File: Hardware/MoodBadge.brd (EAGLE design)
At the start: 112.2 x 114.3 mm, 80 parts, among them IC1 PCF8574T, U2 ATMEGA328P_TQFP, Y1 Crystal-CA-310

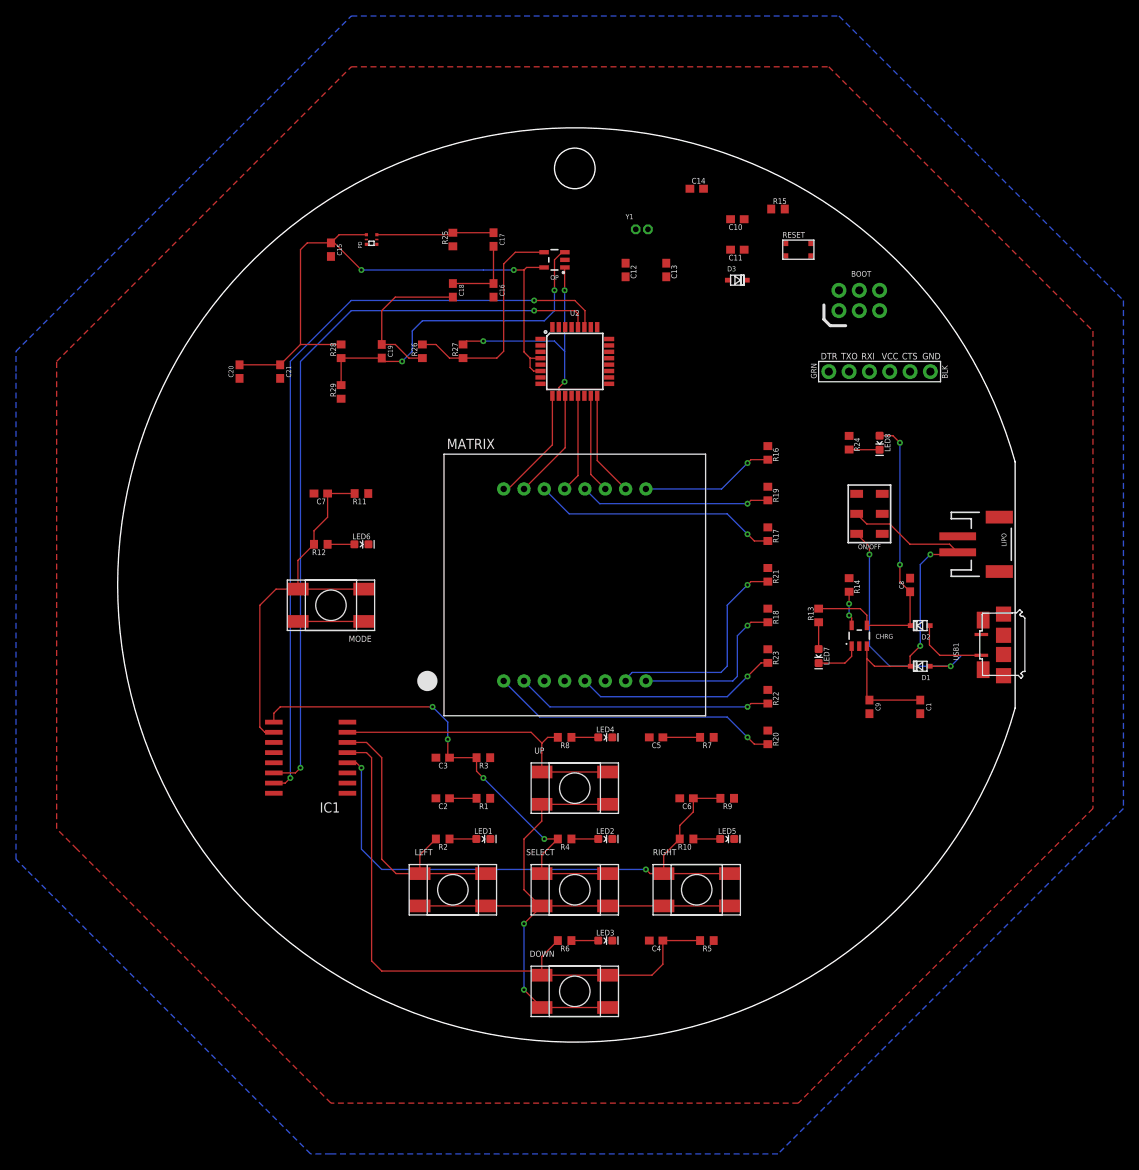
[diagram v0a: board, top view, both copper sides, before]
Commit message: Finished creating traces and filled copper pour
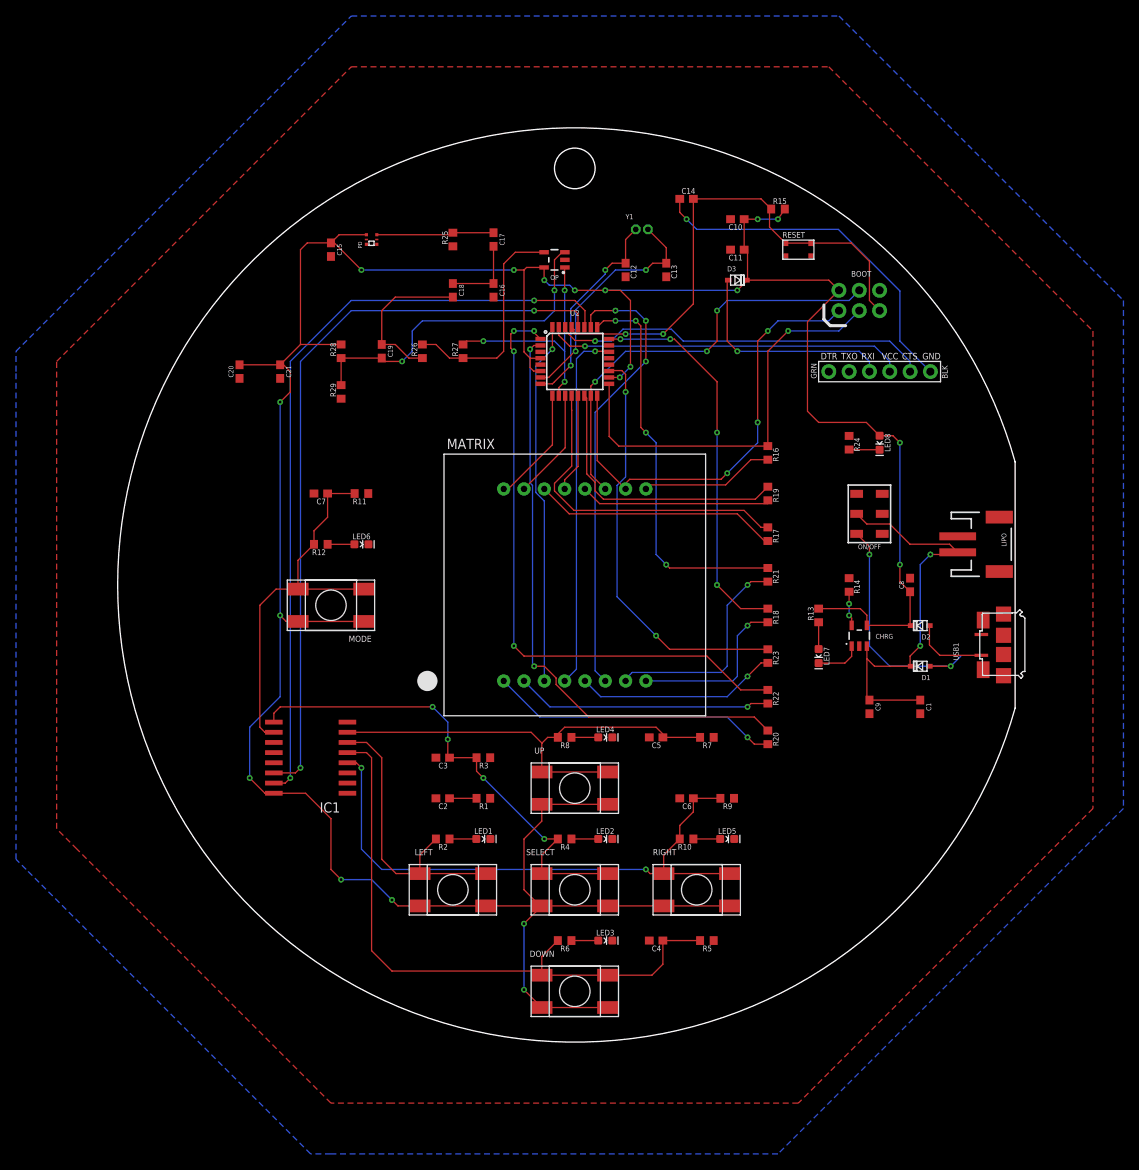
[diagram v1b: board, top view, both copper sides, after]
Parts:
- moved C14 1.80 mm to (14.0, 48.3)
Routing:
- net VCC: track 210.6 -> 395.3 mm, vias 6 -> 19
- net LD2: track 0.00 -> 77.6 mm, vias 0 -> 4
- net LD1: track 0.00 -> 74.3 mm, vias 0 -> 2
- net RESET: track 0.00 -> 64.2 mm, vias 0 -> 2
- net LD6: track 0.00 -> 57.3 mm, vias 0 -> 3
- net LD9: track 0.00 -> 52.3 mm, vias 0 -> 1
- net LD5: track 0.00 -> 52.1 mm, vias 0 -> 2
- net LD7: track 0.00 -> 50.1 mm, vias 0 -> 4
- net LD8: track 0.00 -> 48.7 mm, vias 0 -> 4
- net RXD: track 0.00 -> 47.8 mm, vias 0 -> 1
- net LD3: track 0.00 -> 45.5 mm, vias 0 -> 1
- net LD4: track 0.00 -> 45.4 mm, vias 0 -> 1
- net TXD: track 0.00 -> 45.0 mm, vias 0 -> 1
- net DTR: track 0.00 -> 44.9 mm, vias 0 -> 1
- net LD10: track 13.1 -> 56.9 mm, vias 0 -> 3
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
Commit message: Adjusted trace width and ran DRC
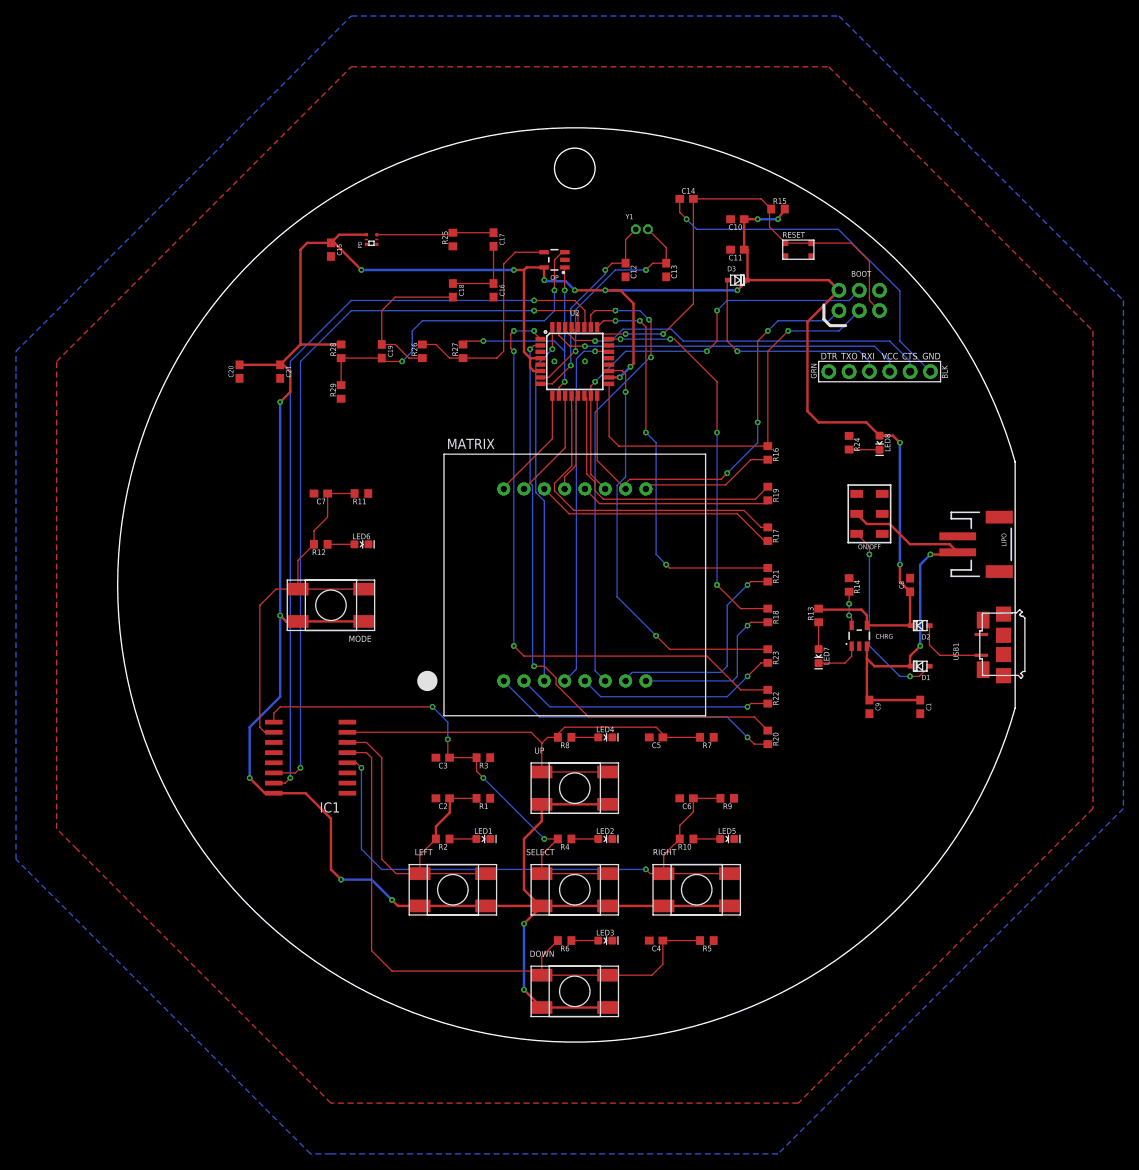
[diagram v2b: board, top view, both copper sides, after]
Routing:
- net N$2: track 30.3 -> 24.3 mm
- net LEFT: track 40.1 -> 45.9 mm
- net LD6: track 57.3 -> 58.2 mm

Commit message: Fixed labeling error for FTDI pins
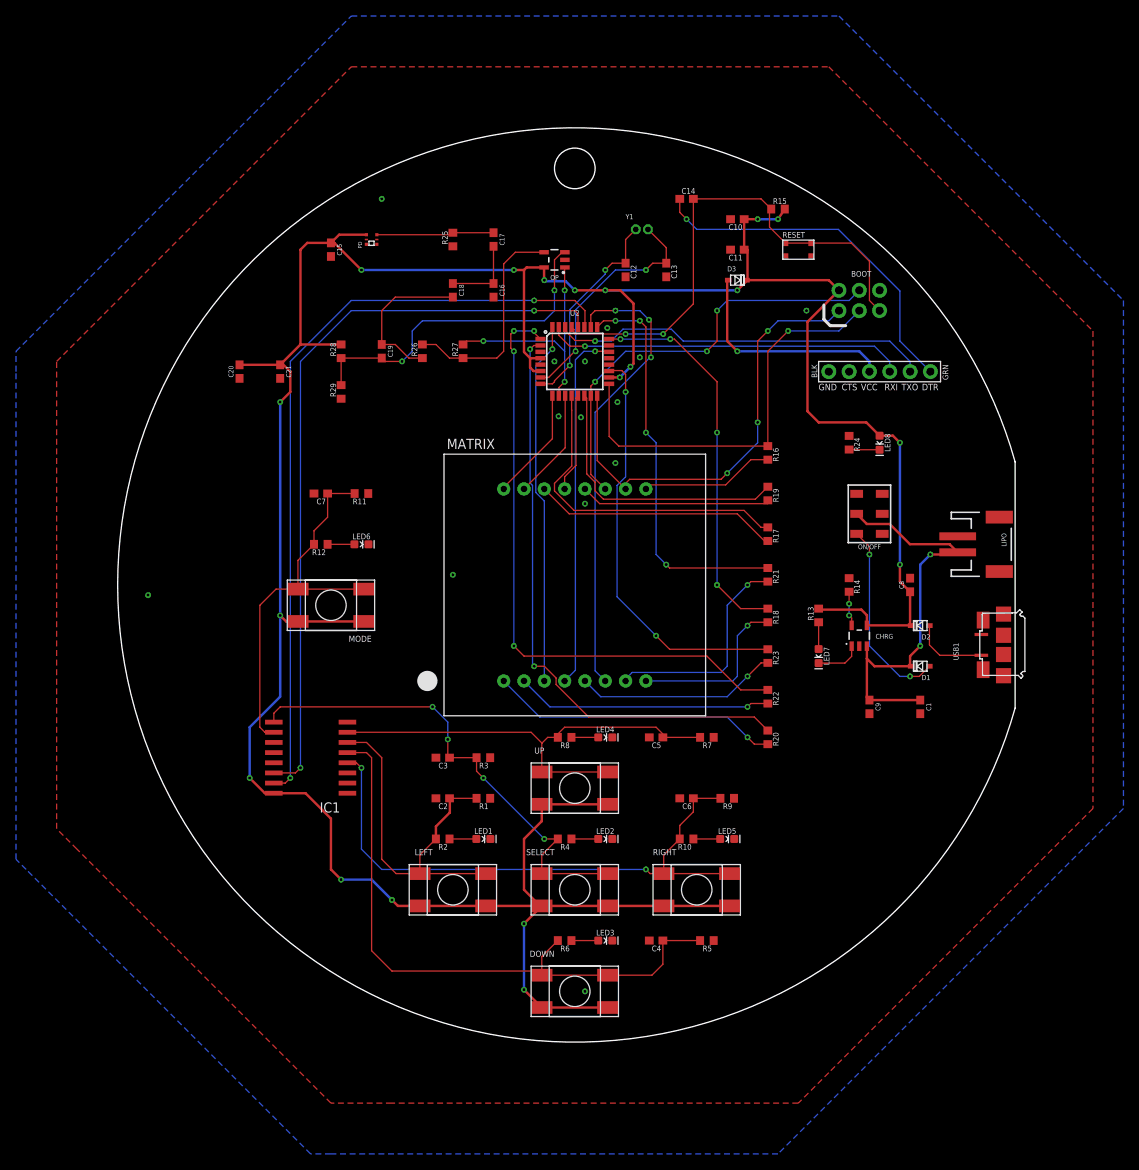
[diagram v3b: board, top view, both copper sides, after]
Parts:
- turned FTDI2 to 180 degrees
- renumbered FTDI1 to FTDI2
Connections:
- net DTR: now also FTDI2.DTR; no longer FTDI2.GND
- net GND: now also FTDI2.CTS, FTDI2.GND; no longer FTDI2.DTR, FTDI2.TXO
- net N$12: now also FTDI2.VCC; no longer FTDI2.RXI
- net RXD: now also FTDI2.TXO; no longer FTDI2.CTS
- net TXD: now also FTDI2.RXI; no longer FTDI2.VCC
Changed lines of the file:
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@@
 <attribute name="VALUE" x="19.05" y="36.435" size="0.635" layer="27"/>
 </element>
-<element name="FTDI1" library="LinnesLab-Connectors" package="FTDI_DEVICE" value="FTDI_DEVICE" x="38.1" y="26.67" smashed="yes"/>
 <element name="BOOT" library="LinnesLab-Connectors" package="2X3-NS" package3d_urn="urn:adsk.eagle:package:18167648/2" value="AVR_SPI_PROG_3X2NS" x="35.56" y="35.56" smashed="yes">
 <attribute name="NAME" x="34.544" y="38.5318" size="0.7112" layer="25" ratio="20"/>
@@
 <attribute name="VALUE" x="-2.54" y="43.18" size="0.6096" layer="27" ratio="20" rot="R180" align="bottom-center"/>
 </element>
+<element name="FTDI2" library="LinnesLab-Connectors" package="FTDI_DEVICE" value="FTDI_DEVICE" x="38.1" y="26.67" smashed="yes" rot="R180"/>
 </elements>
 <signals>
@@
 <contactref element="RESET" pad="3"/>
 <contactref element="RESET" pad="4"/>
-<contactref element="FTDI1" pad="DTR"/>
-<contactref element="FTDI1" pad="TXO"/>
 <contactref element="BOOT" pad="6"/>
 <contactref element="IC1" pad="8"/>
@@
 <via x="-2.54" y="27.94" extent="1-16" drill="0.35"/>
 <via x="1.27" y="27.94" extent="1-16" drill="0.35"/>
+<via x="0.762" y="20.955" extent="1-16" drill="0.35"/>
+<via x="-2.032" y="21.082" extent="1-16" drill="0.35"/>
+<via x="8.128" y="28.448" extent="1-16" drill="0.35"/>
+<via x="5.334" y="22.86" extent="1-16" drill="0.35"/>
+<via x="5.08" y="15.24" extent="1-16" drill="0.35"/>
+<via x="1.27" y="10.16" extent="1-16" drill="0.35"/>
+<via x="4.064" y="32.131" extent="1-16" drill="0.35"/>
+<via x="28.956" y="34.29" extent="1-16" drill="0.35"/>
+<via x="-24.13" y="48.26" extent="1-16" drill="0.35"/>
+<via x="-53.34" y="-1.27" extent="1-16" drill="0.35"/>
+<via x="1.27" y="-50.8" extent="1-16" drill="0.35"/>
+<via x="-15.24" y="1.27" extent="1-16" drill="0.35"/>
+<contactref element="FTDI2" pad="CTS"/>
+<contactref element="FTDI2" pad="GND"/>
 </signal>
 <signal name="VLIPO" class="1">
@@
 <signal name="DTR">
 <contactref element="C14" pad="1"/>
-<contactref element="FTDI1" pad="GND"/>
 <wire x1="13.12" y1="48.26" x2="13.12" y2="46.57" width="0.1524" layer="1"/>
 <wire x1="13.12" y1="46.57" x2="13.97" y2="45.72" width="0.1524" layer="1"/>
@@
 <wire x1="32.94106875" y1="44.45" x2="40.64" y2="36.75106875" width="0.1524" layer="16"/>
 <wire x1="40.64" y1="36.75106875" x2="40.64" y2="30.48" width="0.1524" layer="16"/>
+<contactref element="FTDI2" pad="DTR"/>
 <wire x1="40.64" y1="30.48" x2="44.45" y2="26.67" width="0.1524" layer="16"/>
 </signal>
@@
 <via x="3.81" y="39.37" extent="1-16" drill="0.35"/>
 <wire x1="-4.2926" y1="25.14" x2="-2.8" y2="25.14" width="0.1524" layer="1"/>
-<via x="-0.508" y="27.432" extent="1-16" drill="0.35"/>
-<wire x1="-0.508" y1="27.432" x2="-0.508" y2="34.544" width="0.1524" layer="16"/>
+<via x="-0.635" y="27.432" extent="1-16" drill="0.35"/>
+<wire x1="-0.635" y1="27.432" x2="-0.635" y2="34.417" width="0.1524" layer="16"/>
 <wire x1="-2.8" y1="25.14" x2="-2.54" y2="25.4" width="0.1524" layer="1"/>
-<wire x1="-2.54" y1="25.4" x2="-0.508" y2="27.432" width="0.1524" layer="1"/>
+<wire x1="-0.635" y1="27.432" x2="-2.54" y2="25.527" width="0.1524" layer="1"/>
+<wire x1="-2.54" y1="25.4" x2="-2.54" y2="25.527" width="0.1524" layer="1"/>
 <wire x1="3.81" y1="38.862" x2="3.81" y2="39.37" width="0.1524" layer="16"/>
-<wire x1="3.81" y1="38.862" x2="-0.508" y2="34.544" width="0.1524" layer="16"/>
+<wire x1="3.81" y1="38.862" x2="-0.635" y2="34.417" width="0.1524" layer="16"/>
 </signal>
 <signal name="LD6">
@@
 <via x="2.54" y="29.21" extent="1-16" drill="0.35"/>
 <wire x1="2.54" y1="29.21" x2="1.143" y2="29.21" width="0.1524" layer="16"/>
-<wire x1="0.2032" y1="-10.5268" x2="-1.27" y2="-12" width="0.1524" layer="16"/>
-<wire x1="0.2032" y1="28.2702" x2="0.2032" y2="-10.5268" width="0.1524" layer="16"/>
-<wire x1="1.143" y1="29.21" x2="0.2032" y2="28.2702" width="0.1524" layer="16"/>
+<wire x1="0.0762" y1="-10.6538" x2="-1.27" y2="-12" width="0.1524" layer="16"/>
+<wire x1="0.0762" y1="28.1432" x2="0.0762" y2="-10.6538" width="0.1524" layer="16"/>
+<wire x1="1.143" y1="29.21" x2="0.0762" y2="28.1432" width="0.1524" layer="16"/>
 </signal>
 <signal name="RXD">
 <contactref element="U2" pad="30"/>
-<contactref element="FTDI1" pad="CTS"/>
-<wire x1="41.91" y1="27.94" x2="39.37" y2="30.48" width="0.1524" layer="16"/>
-<wire x1="41.91" y1="27.94" x2="41.91" y2="26.67" width="0.1524" layer="16"/>
+<wire x1="39.37" y1="30.48" x2="41.91" y2="27.94" width="0.1524" layer="16"/>
 <via x="2.54" y="30.48" extent="1-16" drill="0.35"/>
 <wire x1="39.37" y1="30.48" x2="13.55815" y2="30.48" width="0.1524" layer="16"/>
@@
 <wire x1="-1.27" y1="31.75" x2="-1.27" y2="32.1626" width="0.1524" layer="1"/>
 <wire x1="-1.27" y1="32.1626" x2="-1.2" y2="32.2326" width="0.1524" layer="1"/>
+<contactref element="FTDI2" pad="TXO"/>
+<wire x1="41.91" y1="27.94" x2="41.91" y2="26.67" width="0.1524" layer="16"/>
 </signal>
 <signal name="TXD">
 <contactref element="U2" pad="31"/>
-<contactref element="FTDI1" pad="VCC"/>
 <wire x1="-2" y1="32.2326" x2="-2" y2="31.21" width="0.1524" layer="1"/>
 <wire x1="-2" y1="31.21" x2="-0.635" y2="29.845" width="0.1524" layer="1"/>
 <via x="1.27" y="29.845" extent="1-16" drill="0.35"/>
-<wire x1="39.37" y1="27.94" x2="39.37" y2="26.67" width="0.1524" layer="16"/>
-<wire x1="39.37" y1="27.94" x2="37.465" y2="29.845" width="0.1524" layer="16"/>
+<wire x1="37.465" y1="29.845" x2="39.37" y2="27.94" width="0.1524" layer="16"/>
 <wire x1="-0.635" y1="29.845" x2="1.27" y2="29.845" width="0.1524" layer="1"/>
 <wire x1="37.465" y1="29.845" x2="1.27" y2="29.845" width="0.1524" layer="16"/>
+<contactref element="FTDI2" pad="RXI"/>
+<wire x1="39.37" y1="27.94" x2="39.37" y2="26.67" width="0.1524" layer="16"/>
 </signal>
 <signal name="LD3">
@@
 <wire x1="4.2926" y1="18.5674" x2="4.2926" y2="25.14" width="0.1524" layer="1"/>
 </signal>
-<signal name="N$12">
+<signal name="N$12" class="1">
 <contactref element="D3" pad="+"/>
-<contactref element="FTDI1" pad="RXI"/>
-<wire x1="36.83" y1="27.94" x2="35.56" y2="29.21" width="0.1524" layer="16"/>
-<wire x1="36.83" y1="27.94" x2="36.83" y2="26.67" width="0.1524" layer="16"/>
-<wire x1="35.56" y1="29.21" x2="20.32" y2="29.21" width="0.1524" layer="16"/>
+<wire x1="35.56" y1="29.21" x2="36.83" y2="27.94" width="0.3048" layer="16"/>
+<wire x1="35.56" y1="29.21" x2="20.32" y2="29.21" width="0.3048" layer="16"/>
 <via x="20.32" y="29.21" extent="1-16" drill="0.35"/>
-<wire x1="20.32" y1="29.21" x2="19.05" y2="30.48" width="0.1524" layer="1"/>
-<wire x1="19.05" y1="30.48" x2="19.05" y2="37.98" width="0.1524" layer="1"/>
-<wire x1="19.05" y1="37.98" x2="19.17" y2="38.1" width="0.1524" layer="1"/>
+<wire x1="20.32" y1="29.21" x2="19.05" y2="30.48" width="0.3048" layer="1"/>
+<wire x1="19.05" y1="30.48" x2="19.05" y2="37.98" width="0.3048" layer="1"/>
+<wire x1="19.05" y1="37.98" x2="19.17" y2="38.1" width="0.3048" layer="1"/>
+<contactref element="FTDI2" pad="VCC"/>
+<wire x1="36.83" y1="27.94" x2="36.83" y2="26.67" width="0.3048" layer="16"/>
 </signal>
 <signal name="N$14">
